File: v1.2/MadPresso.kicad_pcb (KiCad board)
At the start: 2 copper layers, 108 x 57.5 mm, 75 parts, among them J1 Conn_01x07, J2 Conn_01x03, J3 Conn_01x02, J4 Conn_01x04, Q1 BC847, Q2 BSS84, Q3 T835-600B, Q4 2N7002, Q5 T835-600B, Q6 2N7002, Q7 T835-600B, Q8 2N7002, U1 LTV-356T, U2 ADC101C021CIMK, U3 WeMos_D1_mini, U4 MID400, U5 MID400, U6 TLP160G, U7 TLP160G, U8 TLP160G

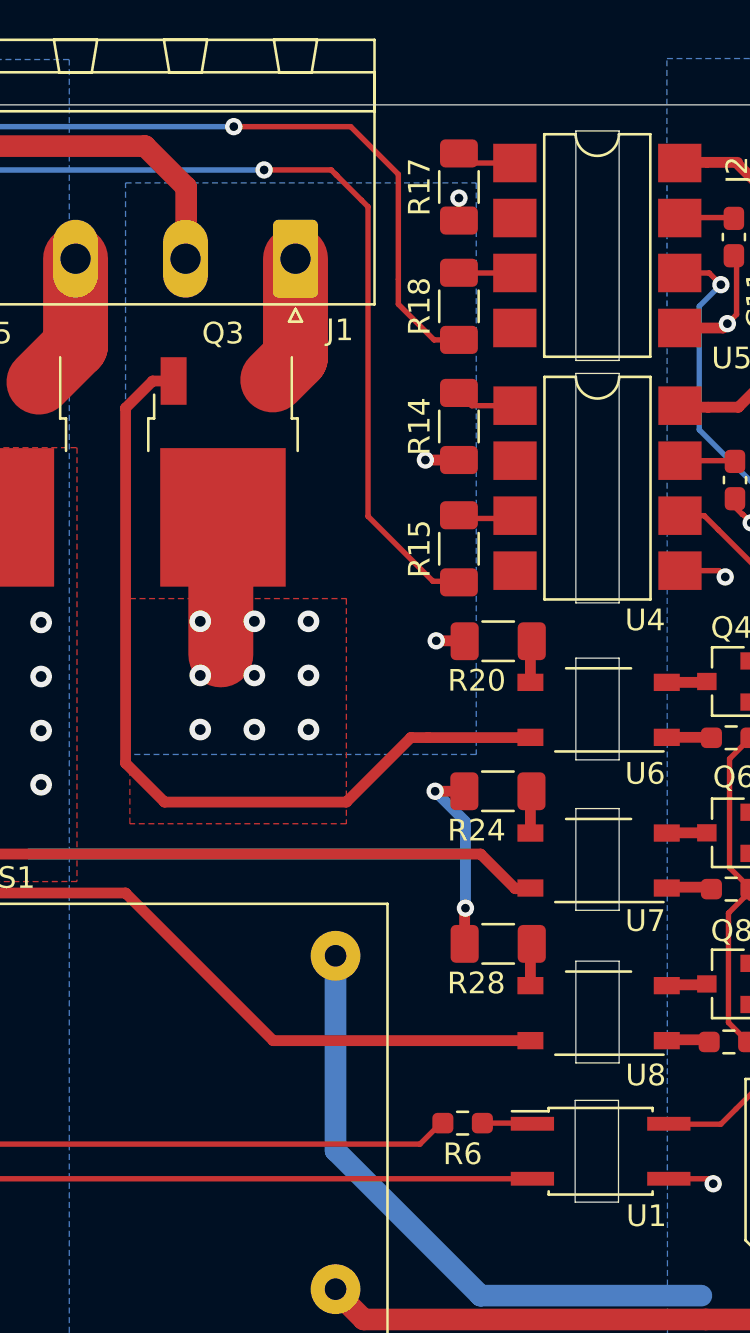
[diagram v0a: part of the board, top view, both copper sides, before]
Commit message: some more vias for neut triac
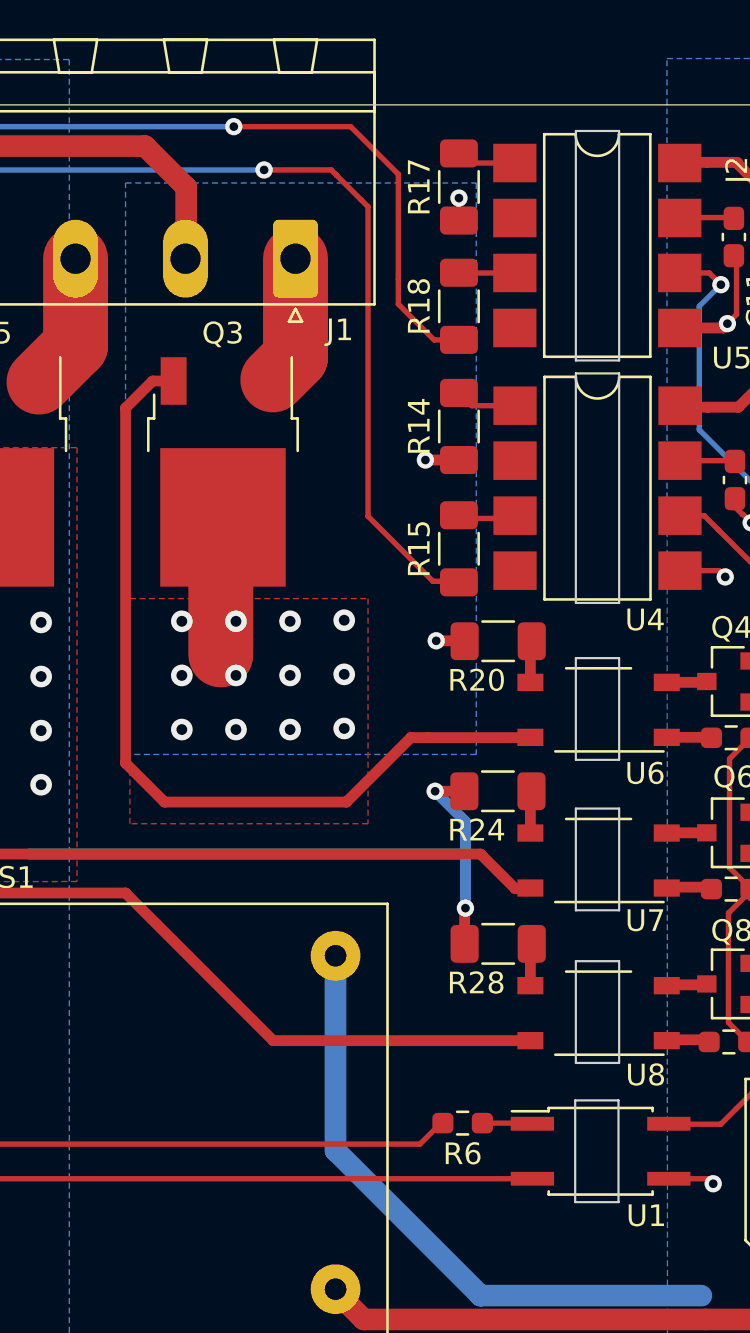
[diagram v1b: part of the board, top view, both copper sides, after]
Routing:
- net NEUT: vias 13 -> 16

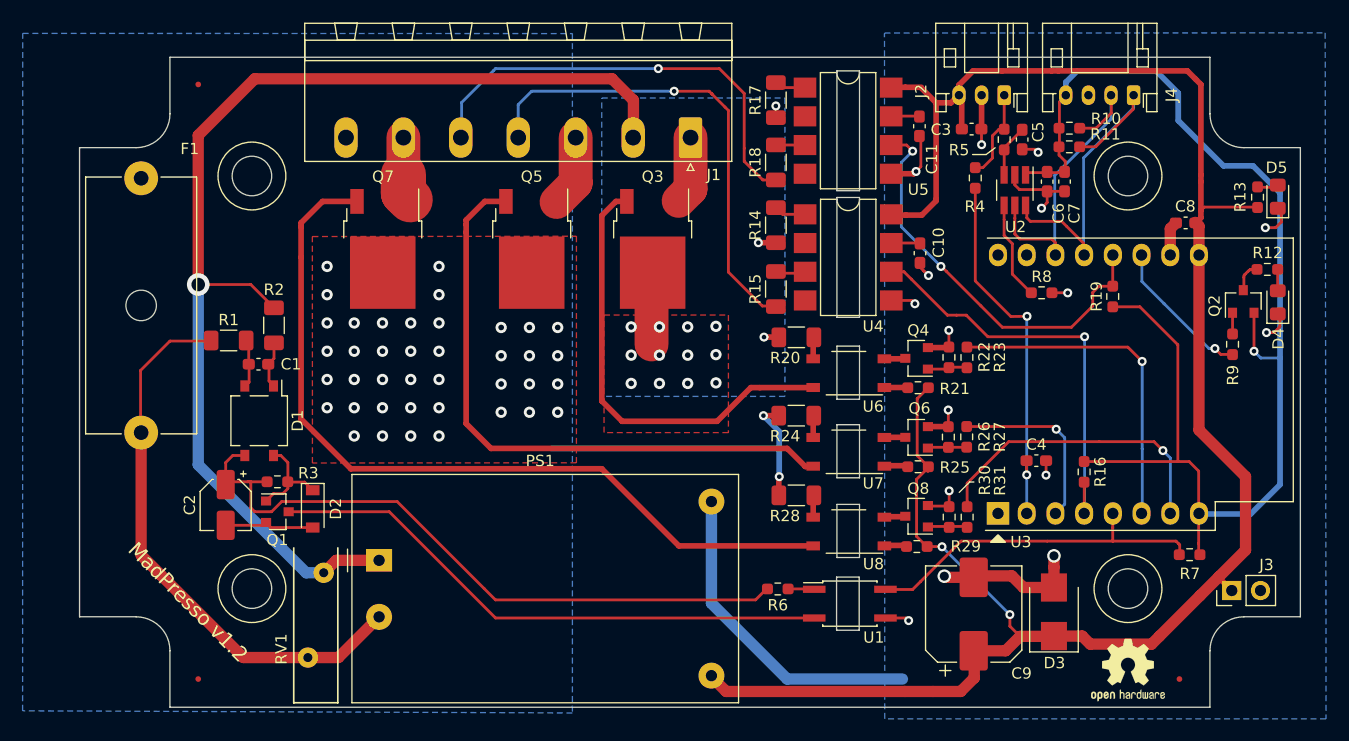
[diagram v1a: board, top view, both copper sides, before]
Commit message: more cleanups, replace caps with ceramic types, polygon updates
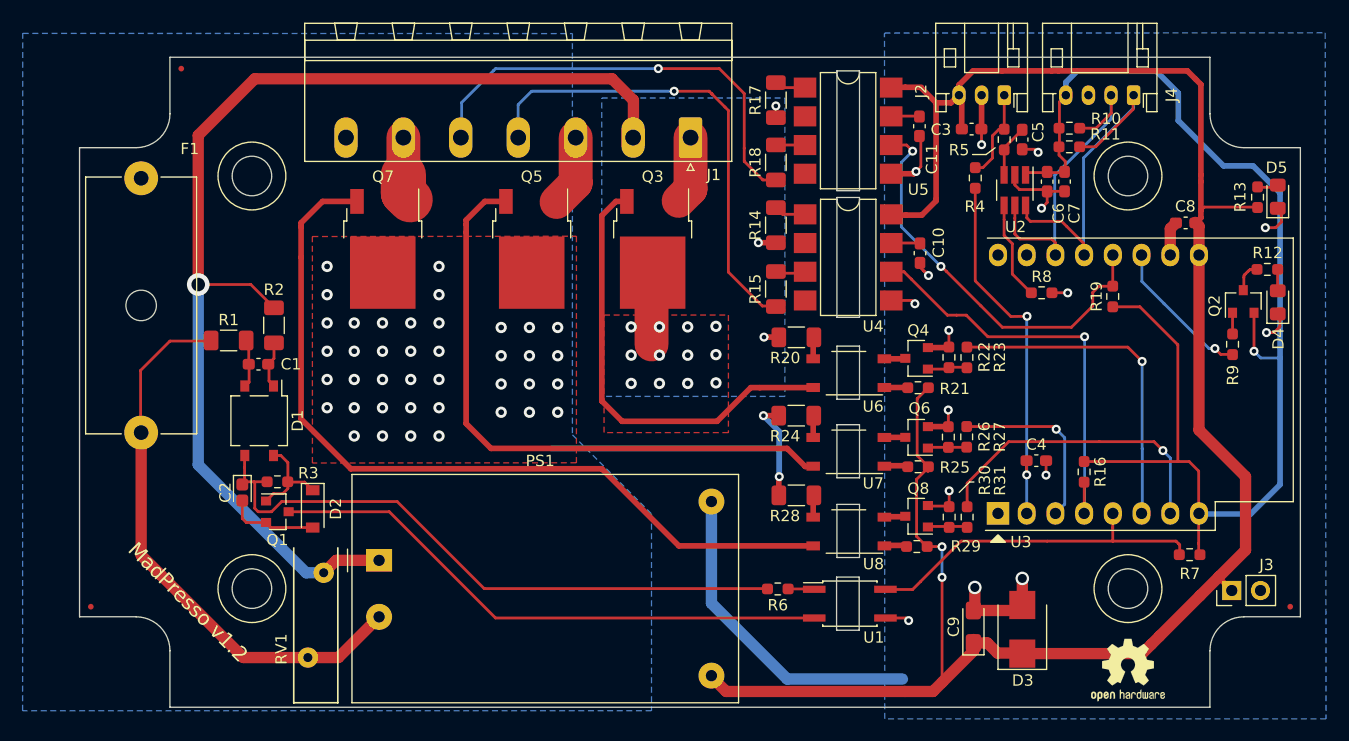
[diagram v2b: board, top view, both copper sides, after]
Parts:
- C2: footprint Capacitor_SMD:CP_Elec_4x5.8 -> Capacitor_Tantalum_SMD:CP_EIA-1608-08_AVX-J
- C9: value 150uF -> 100uF; footprint Capacitor_SMD:CP_Elec_8x10 -> Capacitor_Tantalum_SMD:CP_EIA-3216-18_Kemet-A_Pad1.58x1.35mm_HandSolder
- moved FID3 11.7 mm to (107.1, 48.6)
- moved FID2 11.5 mm to (1.00, 48.6)
- moved D3 3.20 mm to (83.4, 50.6)
- moved FID1 2.05 mm to (9.00, 1.00)
- moved C2 1.84 mm to (14.4, 38.5)
- moved C9 1.13 mm to (79.1, 50.4)
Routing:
- net Net-(C2-Pad1): track 60.5 -> 56.4 mm
- net GND: track 89.0 -> 85.1 mm
- net +5V: track 181.3 -> 182.1 mm

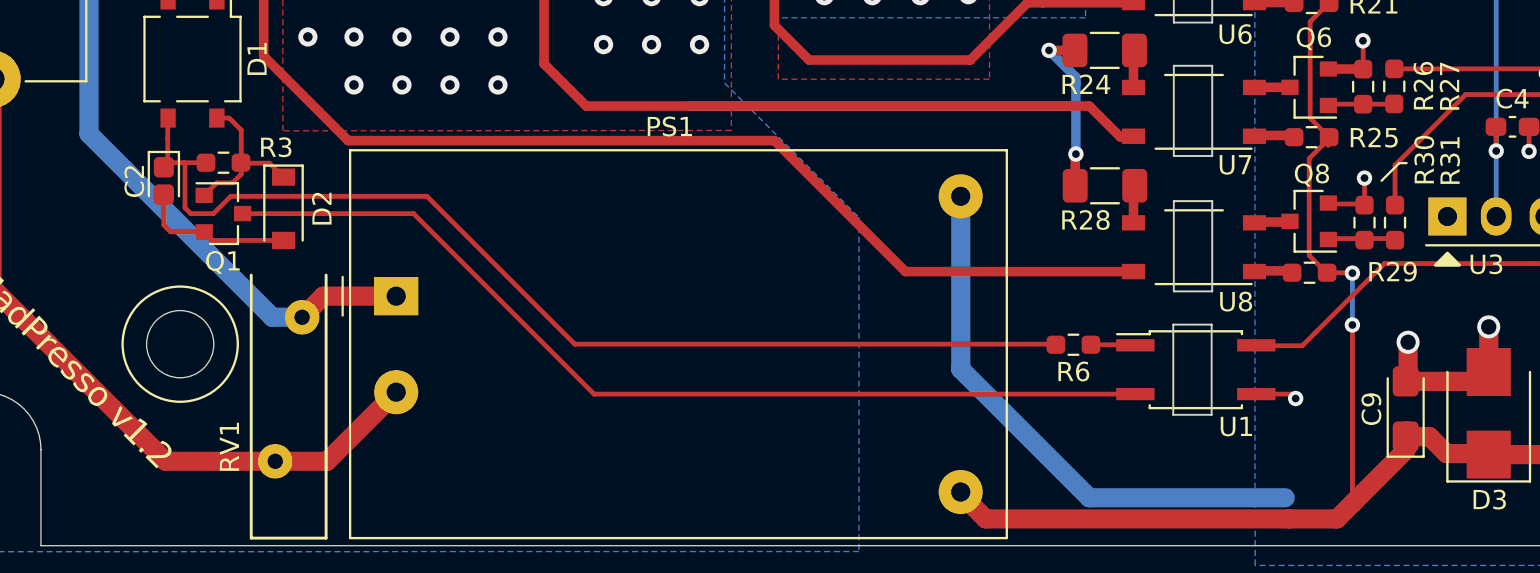
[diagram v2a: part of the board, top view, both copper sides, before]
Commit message: switch to ceramic caps
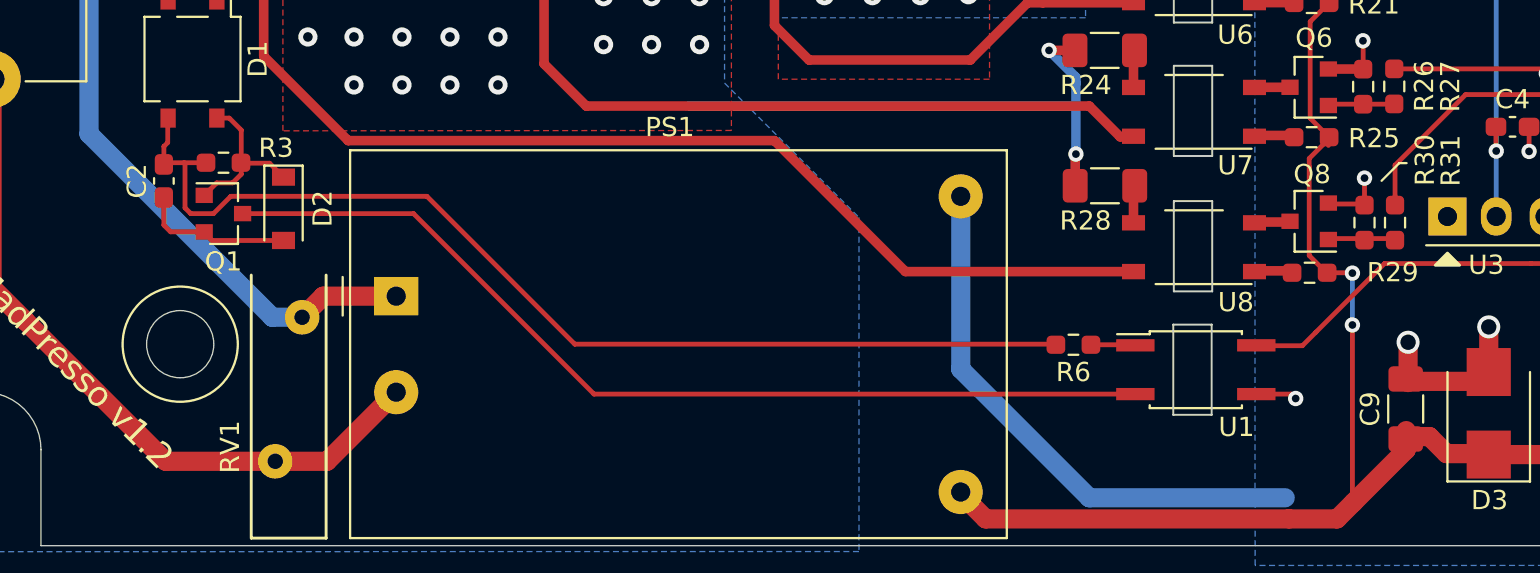
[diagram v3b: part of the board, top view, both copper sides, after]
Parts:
- C2: footprint Capacitor_Tantalum_SMD:CP_EIA-1608-08_AVX-J -> Capacitor_SMD:C_0603_1608Metric_Pad1.08x0.95mm_HandSolder
- C9: footprint Capacitor_Tantalum_SMD:CP_EIA-3216-18_Kemet-A_Pad1.58x1.35mm_HandSolder -> Capacitor_SMD:C_1206_3216Metric_Pad1.33x1.80mm_HandSolder
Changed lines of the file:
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@@
     )
   )
-  (footprint "Capacitor_Tantalum_SMD:CP_EIA-3216-18_Kemet-A_Pad1.58x1.35mm_HandSolder" (layer "F.Cu")
+  (footprint "Capacitor_SMD:C_1206_3216Metric_Pad1.33x1.80mm_HandSolder" (layer "F.Cu")
     (at 79.075 50.375 90)
-    (descr "Tantalum Capacitor SMD Kemet-A (3216-18 Metric), IPC_7351 nominal, (Body size from: http://www.kemet.com/Lists/ProductCatalog/Attachments/253/KEM_TC101_STD.pdf), generated with kicad-footprint-generator")
-    (tags "capacitor tantalum")
+    (descr "Capacitor SMD 1206 (3216 Metric), square (rectangular) end terminal, IPC_7351 nominal with elongated pad for handsoldering. (Body size source: IPC-SM-782 page 76, https://www.pcb-3d.com/wordpress/wp-content/uploads/ipc-sm-782a_amendment_1_and_2.pdf), generated with kicad-footprint-generator")
+    (tags "capacitor handsolder")
     (property "Sheet file" "MadPresso.kicad_sch")
     (property "Sheet name" "")
     (attr smd)
-    (fp_text reference "C9" (at 0 -1.75 90) (layer "F.SilkS")
+    (fp_text reference "C9" (at 0 -1.85 90) (layer "F.SilkS")
       (effects (font (size 1 1) (thickness 0.15)))
     )
-    (fp_text value "100uF" (at 0 1.75 90) (layer "F.Fab")
+    (fp_text value "100uF" (at 0 1.85 90) (layer "F.Fab") hide
       (effects (font (size 1 1) (thickness 0.15)))
     )
@@
       (effects (font (size 0.8 0.8) (thickness 0.12)))
     )
-    (fp_line (start -2.485 0.935) (end 1.6 0.935) (layer "F.SilkS") (width 0.12))
-    (fp_line (start 1.6 -0.935) (end -2.485 -0.935) (layer "F.SilkS") (width 0.12))
-    (fp_line (start -2.485 -0.935) (end -2.485 0.935) (layer "F.SilkS") (width 0.12))
-    (fp_line (start 2.48 1.05) (end -2.48 1.05) (layer "F.CrtYd") (width 0.05))
-    (fp_line (start -2.48 1.05) (end -2.48 -1.05) (layer "F.CrtYd") (width 0.05))
-    (fp_line (start 2.48 -1.05) (end 2.48 1.05) (layer "F.CrtYd") (width 0.05))
-    (fp_line (start -2.48 -1.05) (end 2.48 -1.05) (layer "F.CrtYd") (width 0.05))
-    (fp_line (start -1.6 0.8) (end 1.6 0.8) (layer "F.Fab") (width 0.1))
-    (fp_line (start -1.6 -0.4) (end -1.6 0.8) (layer "F.Fab") (width 0.1))
-    (fp_line (start -1.2 -0.8) (end -1.6 -0.4) (layer "F.Fab") (width 0.1))
-    (fp_line (start 1.6 -0.8) (end -1.2 -0.8) (layer "F.Fab") (width 0.1))
-    (fp_line (start 1.6 0.8) (end 1.6 -0.8) (layer "F.Fab") (width 0.1))
-    (pad "1" smd roundrect (at -1.4375 0 90) (size 1.575 1.35) (layers "F.Cu" "F.Paste" "F.Mask") (roundrect_rratio 0.185185)
+    (fp_line (start -0.711252 0.91) (end 0.711252 0.91) (layer "F.SilkS") (width 0.12))
+    (fp_line (start -0.711252 -0.91) (end 0.711252 -0.91) (layer "F.SilkS") (width 0.12))
+    (fp_line (start -2.48 1.15) (end -2.48 -1.15) (layer "F.CrtYd") (width 0.05))
+    (fp_line (start -2.48 -1.15) (end 2.48 -1.15) (layer "F.CrtYd") (width 0.05))
+    (fp_line (start 2.48 1.15) (end -2.48 1.15) (layer "F.CrtYd") (width 0.05))
+    (fp_line (start 2.48 -1.15) (end 2.48 1.15) (layer "F.CrtYd") (width 0.05))
+    (fp_line (start -1.6 -0.8) (end 1.6 -0.8) (layer "F.Fab") (width 0.1))
+    (fp_line (start 1.6 0.8) (end -1.6 0.8) (layer "F.Fab") (width 0.1))
+    (fp_line (start 1.6 -0.8) (end 1.6 0.8) (layer "F.Fab") (width 0.1))
+    (fp_line (start -1.6 0.8) (end -1.6 -0.8) (layer "F.Fab") (width 0.1))
+    (pad "1" smd roundrect (at -1.5625 0 90) (size 1.325 1.8) (layers "F.Cu" "F.Paste" "F.Mask") (roundrect_rratio 0.188679)
       (net 8 "+5V"))
-    (pad "2" smd roundrect (at 1.4375 0 90) (size 1.575 1.35) (layers "F.Cu" "F.Paste" "F.Mask") (roundrect_rratio 0.185185)
+    (pad "2" smd roundrect (at 1.5625 0 90) (size 1.325 1.8) (layers "F.Cu" "F.Paste" "F.Mask") (roundrect_rratio 0.188679)
       (net 1 "GND"))
-    (model "${KISYS3DMOD}/Capacitor_Tantalum_SMD.3dshapes/CP_EIA-3216-18_Kemet-A.wrl"
+    (model "${KISYS3DMOD}/Capacitor_SMD.3dshapes/C_1206_3216Metric.wrl"
       (offset (xyz 0 0 0))
       (scale (xyz 1 1 1))
@@
     )
   )
-  (footprint "Capacitor_Tantalum_SMD:CP_EIA-1608-08_AVX-J" (layer "F.Cu")
+  (footprint "Capacitor_SMD:C_0603_1608Metric_Pad1.08x0.95mm_HandSolder" (layer "F.Cu")
     (at 14.4 38.5 -90)
-    (descr "Tantalum Capacitor SMD AVX-J (1608-08 Metric), IPC_7351 nominal, (Body size from: https://www.vishay.com/docs/48064/_t58_vmn_pt0471_1601.pdf), generated with kicad-footprint-generator")
-    (tags "capacitor tantalum")
+    (descr "Capacitor SMD 0603 (1608 Metric), square (rectangular) end terminal, IPC_7351 nominal with elongated pad for handsoldering. (Body size source: IPC-SM-782 page 76, https://www.pcb-3d.com/wordpress/wp-content/uploads/ipc-sm-782a_amendment_1_and_2.pdf), generated with kicad-footprint-generator")
+    (tags "capacitor handsolder")
     (property "Sheet file" "MadPresso.kicad_sch")
     (property "Sheet name" "")
     (attr smd)
-    (fp_text reference "C2" (at 0 1.5 -90) (layer "F.SilkS")
+    (fp_text reference "C2" (at 0 1.4 -90) (layer "F.SilkS")
       (effects (font (size 1 1) (thickness 0.15)))
     )
-    (fp_text value "10uF" (at 0 1.48 -90) (layer "F.Fab") hide
+    (fp_text value "10uF" (at 0 1.43 -90) (layer "F.Fab") hide
       (effects (font (size 1 1) (thickness 0.15)))
     )
@@
       (effects (font (size 0.4 0.4) (thickness 0.06)))
     )
-    (fp_line (start -1.51 -0.785) (end -1.51 0.785) (layer "F.SilkS") (width 0.12))
-    (fp_line (start -1.51 0.785) (end 0.8 0.785) (layer "F.SilkS") (width 0.12))
-    (fp_line (start 0.8 -0.785) (end -1.51 -0.785) (layer "F.SilkS") (width 0.12))
-    (fp_line (start 1.5 -0.78) (end 1.5 0.78) (layer "F.CrtYd") (width 0.05))
-    (fp_line (start 1.5 0.78) (end -1.5 0.78) (layer "F.CrtYd") (width 0.05))
-    (fp_line (start -1.5 -0.78) (end 1.5 -0.78) (layer "F.CrtYd") (width 0.05))
-    (fp_line (start -1.5 0.78) (end -1.5 -0.78) (layer "F.CrtYd") (width 0.05))
-    (fp_line (start -0.8 -0.125) (end -0.8 0.425) (layer "F.Fab") (width 0.1))
-    (fp_line (start 0.8 0.425) (end 0.8 -0.425) (layer "F.Fab") (width 0.1))
-    (fp_line (start -0.8 0.425) (end 0.8 0.425) (layer "F.Fab") (width 0.1))
-    (fp_line (start -0.5 -0.425) (end -0.8 -0.125) (layer "F.Fab") (width 0.1))
-    (fp_line (start 0.8 -0.425) (end -0.5 -0.425) (layer "F.Fab") (width 0.1))
-    (pad "1" smd roundrect (at -0.7125 0 270) (size 1.075 1.05) (layers "F.Cu" "F.Paste" "F.Mask") (roundrect_rratio 0.238095)
+    (fp_line (start -0.146267 -0.51) (end 0.146267 -0.51) (layer "F.SilkS") (width 0.12))
+    (fp_line (start -0.146267 0.51) (end 0.146267 0.51) (layer "F.SilkS") (width 0.12))
+    (fp_line (start -1.65 0.73) (end -1.65 -0.73) (layer "F.CrtYd") (width 0.05))
+    (fp_line (start 1.65 -0.73) (end 1.65 0.73) (layer "F.CrtYd") (width 0.05))
+    (fp_line (start 1.65 0.73) (end -1.65 0.73) (layer "F.CrtYd") (width 0.05))
+    (fp_line (start -1.65 -0.73) (end 1.65 -0.73) (layer "F.CrtYd") (width 0.05))
+    (fp_line (start -0.8 0.4) (end -0.8 -0.4) (layer "F.Fab") (width 0.1))
+    (fp_line (start 0.8 0.4) (end -0.8 0.4) (layer "F.Fab") (width 0.1))
+    (fp_line (start 0.8 -0.4) (end 0.8 0.4) (layer "F.Fab") (width 0.1))
+    (fp_line (start -0.8 -0.4) (end 0.8 -0.4) (layer "F.Fab") (width 0.1))
+    (pad "1" smd roundrect (at -0.8625 0 270) (size 1.075 0.95) (layers "F.Cu" "F.Paste" "F.Mask") (roundrect_rratio 0.25)
       (net 31 "Net-(C2-Pad1)"))
-    (pad "2" smd roundrect (at 0.7125 0 270) (size 1.075 1.05) (layers "F.Cu" "F.Paste" "F.Mask") (roundrect_rratio 0.238095)
+    (pad "2" smd roundrect (at 0.8625 0 270) (size 1.075 0.95) (layers "F.Cu" "F.Paste" "F.Mask") (roundrect_rratio 0.25)
       (net 30 "Net-(C2-Pad2)"))
-    (model "${KISYS3DMOD}/Capacitor_Tantalum_SMD.3dshapes/CP_EIA-1608-08_AVX-J.wrl"
+    (model "${KISYS3DMOD}/Capacitor_SMD.3dshapes/C_0603_1608Metric.wrl"
       (offset (xyz 0 0 0))
       (scale (xyz 1 1 1))
@@
   (segment (start 20.63 41.6) (end 16.9 41.6) (width 0.25) (layer "F.Cu") (net 30))
   (segment (start 35.8 47) (end 60.8 47) (width 0.25) (layer "F.Cu") (net 31))
-  (segment (start 14.6 36.3) (end 14.6 37.5) (width 0.25) (layer "F.Cu") (net 31))
   (segment (start 15.5 39.9) (end 15.5 37.6) (width 0.25) (layer "F.Cu") (net 31))
+  (segment (start 14.6 36.5) (end 14.6 35.3) (width 0.25) (layer "F.Cu") (net 31))
   (segment (start 16.985002 40.2) (end 17.885002 39.3) (width 0.25) (layer "F.Cu") (net 31))
   (segment (start 14.6 37.5) (end 14.4 37.7) (width 0.25) (layer "F.Cu") (net 31))
   (segment (start 14.45 37.55) (end 14.4 37.5) (width 0.25) (layer "F.Cu") (net 31))
+  (segment (start 14.4 37.6375) (end 14.4 36.7) (width 0.25) (layer "F.Cu") (net 31))
   (segment (start 16.5925 37.55) (end 15.45 37.55) (width 0.25) (layer "F.Cu") (net 31))
   (segment (start 60.895 47.03) (end 60.895 47.28) (width 0.25) (layer "F.Cu") (net 31))
-  (segment (start 14.6 36.3) (end 14.6 35.2) (width 0.25) (layer "F.Cu") (net 31))
   (segment (start 15.8 40.2) (end 15.5 39.9) (width 0.25) (layer "F.Cu") (net 31))
   (segment (start 15.45 37.55) (end 14.45 37.55) (width 0.25) (layer "F.Cu") (net 31))
@@
   (segment (start 17.885002 39.3) (end 28.1 39.3) (width 0.25) (layer "F.Cu") (net 31))
   (segment (start 14.66 35.225) (end 14.63 35.255) (width 0.25) (layer "F.Cu") (net 31))
+  (segment (start 14.4 36.7) (end 14.6 36.5) (width 0.25) (layer "F.Cu") (net 31))
   (segment (start 15.8 40.2) (end 16.985002 40.2) (width 0.25) (layer "F.Cu") (net 31))
   (segment (start 71.9 5.2) (end 71.8 5.1) (width 0.25) (layer "F.Cu") (net 32))
